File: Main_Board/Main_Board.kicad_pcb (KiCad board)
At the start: 4 copper layers, 45 x 38.4 mm, 124 parts, among them IC1 TPS25200DRVR, J1 RESET, J2 MAIN_UART, J3 Baterry input, J4 External bords interfaces, J7 Terminal, J8 Terminal, Q1 2N7002, Q10 FDN339AN, Q7 MMBT3904LT1G, Q8 FDN339AN, Q9 MMBT3904LT1G, U1 W25Q128JVS, U2 ESP32-S3-MINI-1U, U3 TPS63031DSK, U4 TPS63031DSK, U5 TLV61070ADBV, U6 SS351AT, U7 THVD1450DR

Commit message: Keep out zones, cleanup
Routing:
- net +3V3_MB: track 60.0 -> 18.1 mm
- net GND: track 48.4 -> 45.4 mm
- net Net-(Q8-G): track 33.3 -> 31.0 mm
- net /PSU/Back_Boost1/V_In: track 46.9 -> 45.6 mm

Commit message: Routing + cleanup
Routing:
- net Net-(J4-Pin_1): track 16.3 -> 31.9 mm
- net Net-(U2-RXD0): track 0.00 -> 13.6 mm
- net Net-(U2-TXD0): track 0.00 -> 11.7 mm
- net /ESP32/PYRO2_CONTINUITY: track 2.17 -> 10.2 mm, vias 0 -> 1
- net +3V3_MB: track 18.1 -> 21.6 mm, vias 8 -> 12
- net GND: track 45.4 -> 46.9 mm, vias 23 -> 26
- net Net-(Q10-G): track 32.7 -> 31.9 mm

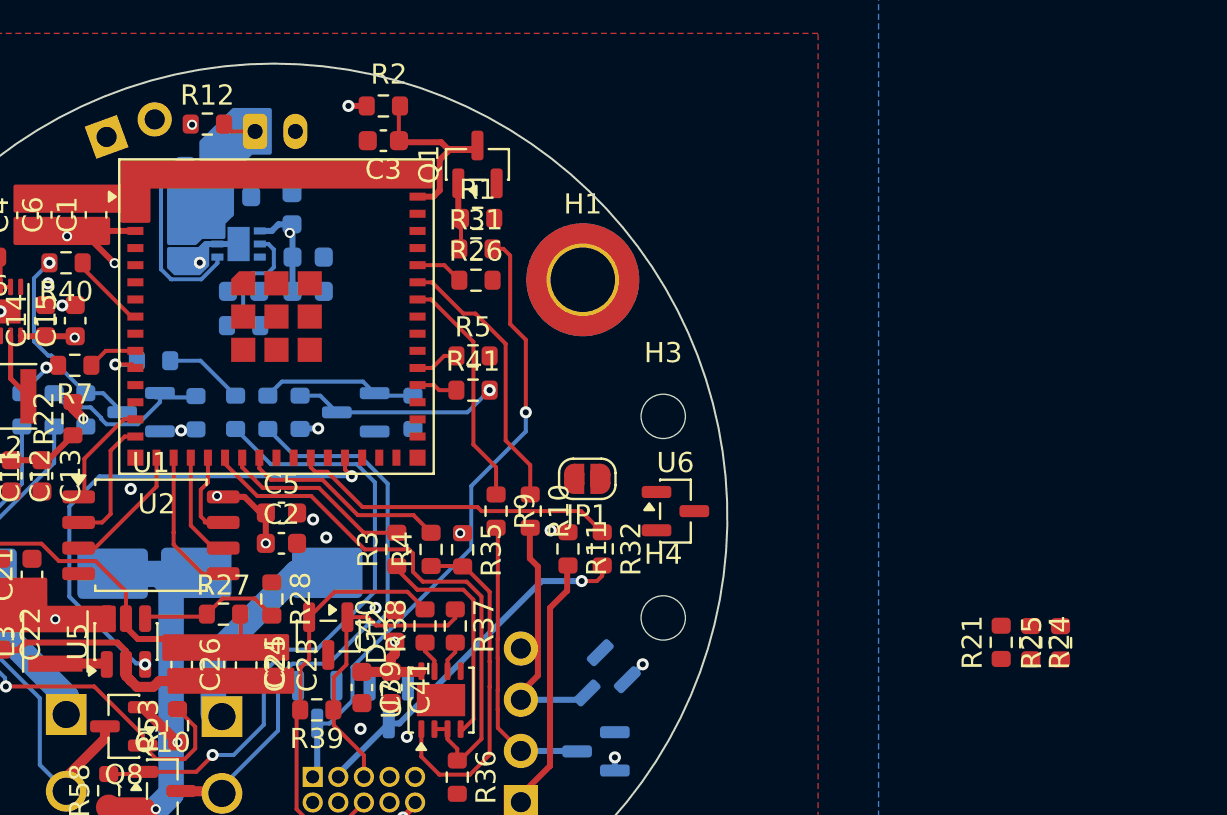
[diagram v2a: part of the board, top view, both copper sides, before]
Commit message: Schematic cleanup, ALED footprint + 3D + sch
+ layout and routing
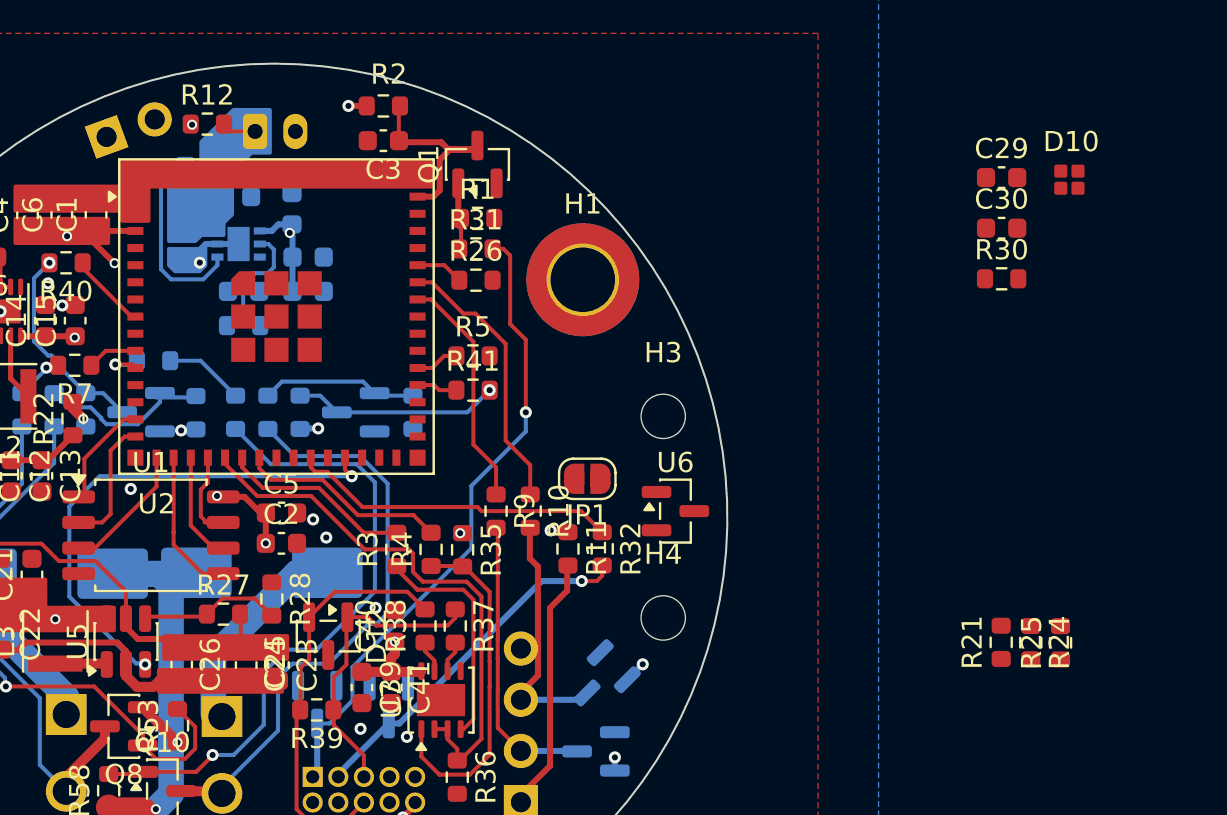
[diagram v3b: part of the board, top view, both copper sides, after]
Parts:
- added C29: 100nF, Capacitor_SMD:C_0603_1608Metric, F.Cu at (136.1, 83.2)
- added C30: 10uF, Capacitor_SMD:C_0603_1608Metric, F.Cu at (136.1, 85.7)
- added D10: SK6812-1515, sk6805-1515:sk68015-1515, F.Cu at (139.5, 83.3)
- added R30: 470R, Resistor_SMD:R_0603_1608Metric, F.Cu at (136.1, 88.2)
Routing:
- net GND: track 46.9 -> 51.3 mm

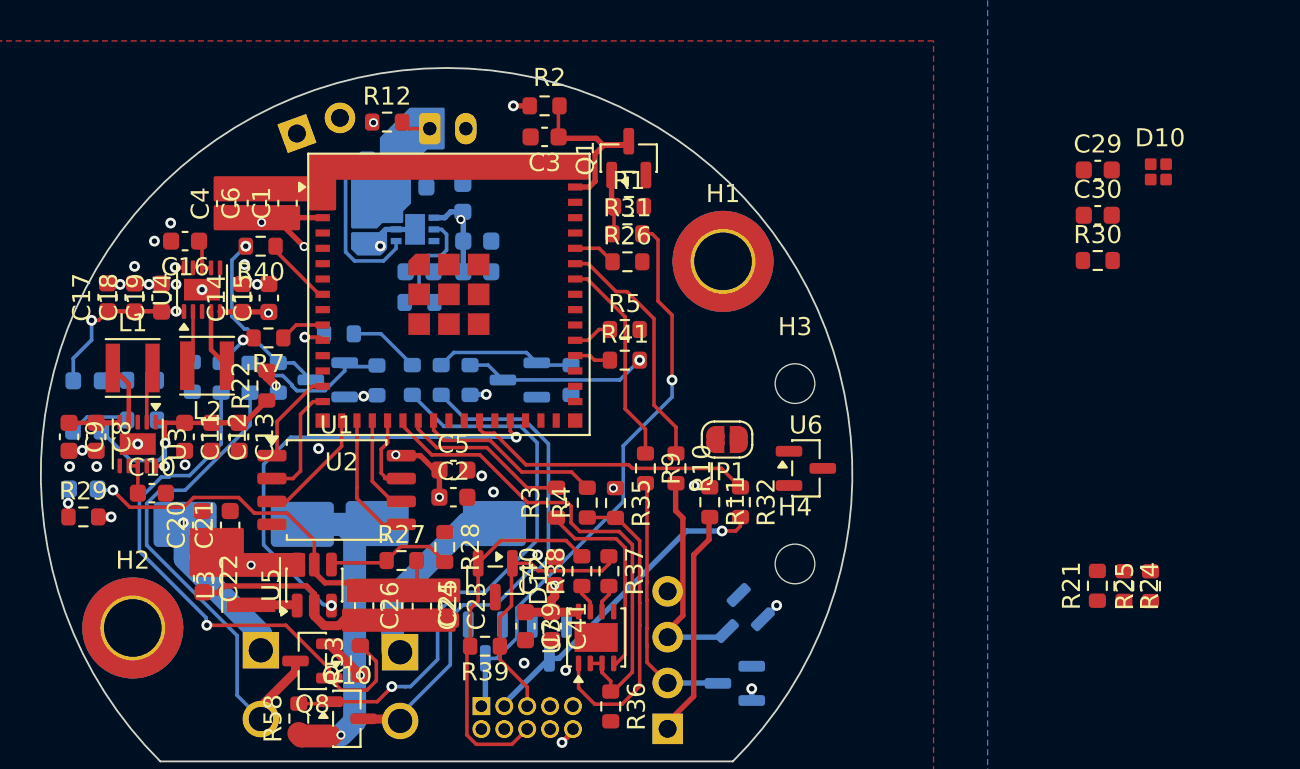
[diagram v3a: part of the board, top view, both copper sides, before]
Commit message: Power routing
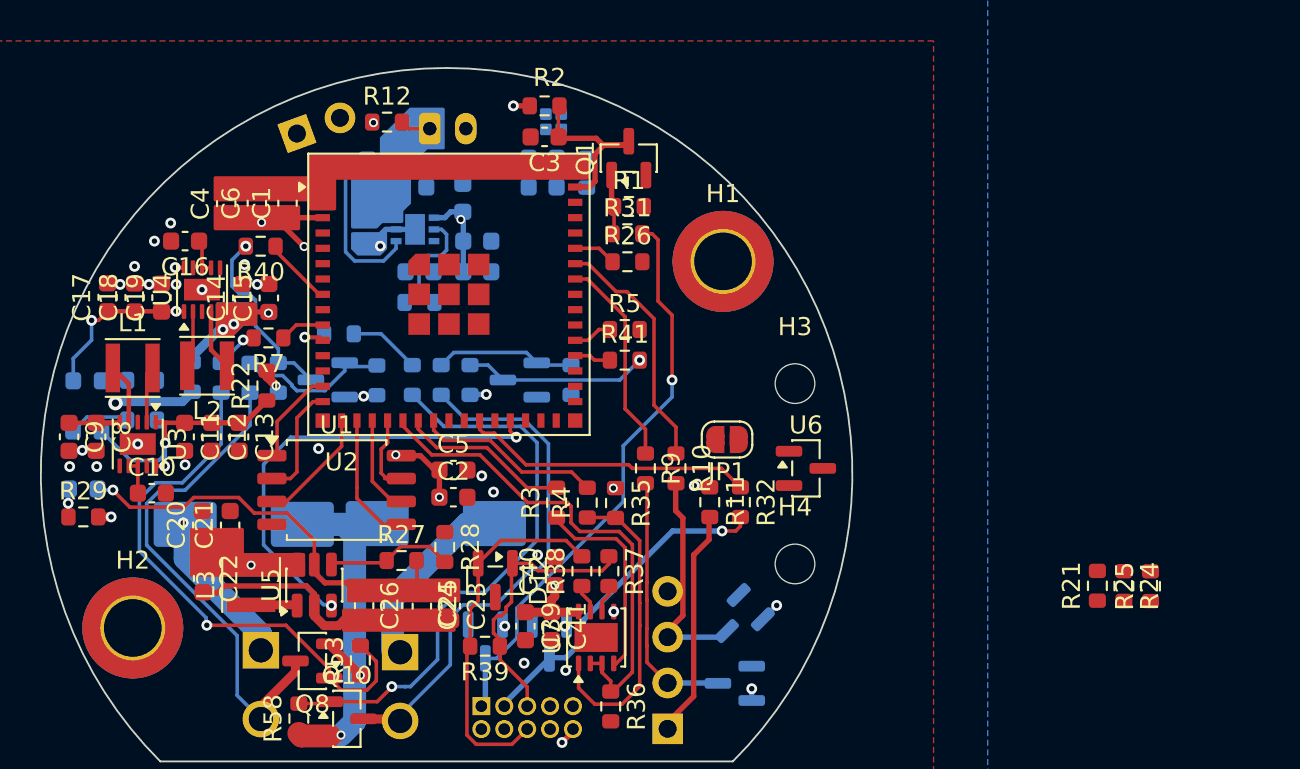
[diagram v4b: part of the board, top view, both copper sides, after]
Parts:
- C29, C30, D10, R30: moved to B.Cu
- moved D10 33.7 mm to (105.9, 80.5)
- moved C30 30.8 mm to (105.3, 84.1), turned to 180 degrees
- moved C29 30.8 mm to (105.3, 82.5), turned to 180 degrees
- moved R30 28.8 mm to (107.8, 83.3), turned to 90 degrees
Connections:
- net Net-(U1-~{HOLD}/~{RESET}/IO_{3}) renamed /ESP32/IO3 / HOLD
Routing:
- net +3V3: track 0.00 -> 8.51 mm, vias 0 -> 2
- net VBUS: track 66.4 -> 70.9 mm, vias 2 -> 3
- net /PSU/Back_Boost1/V_In: track 45.6 -> 49.2 mm, vias 3 -> 5
- net Net-(J4-Pin_3): track 17.9 -> 18.7 mm
- net GND: vias 26 -> 27

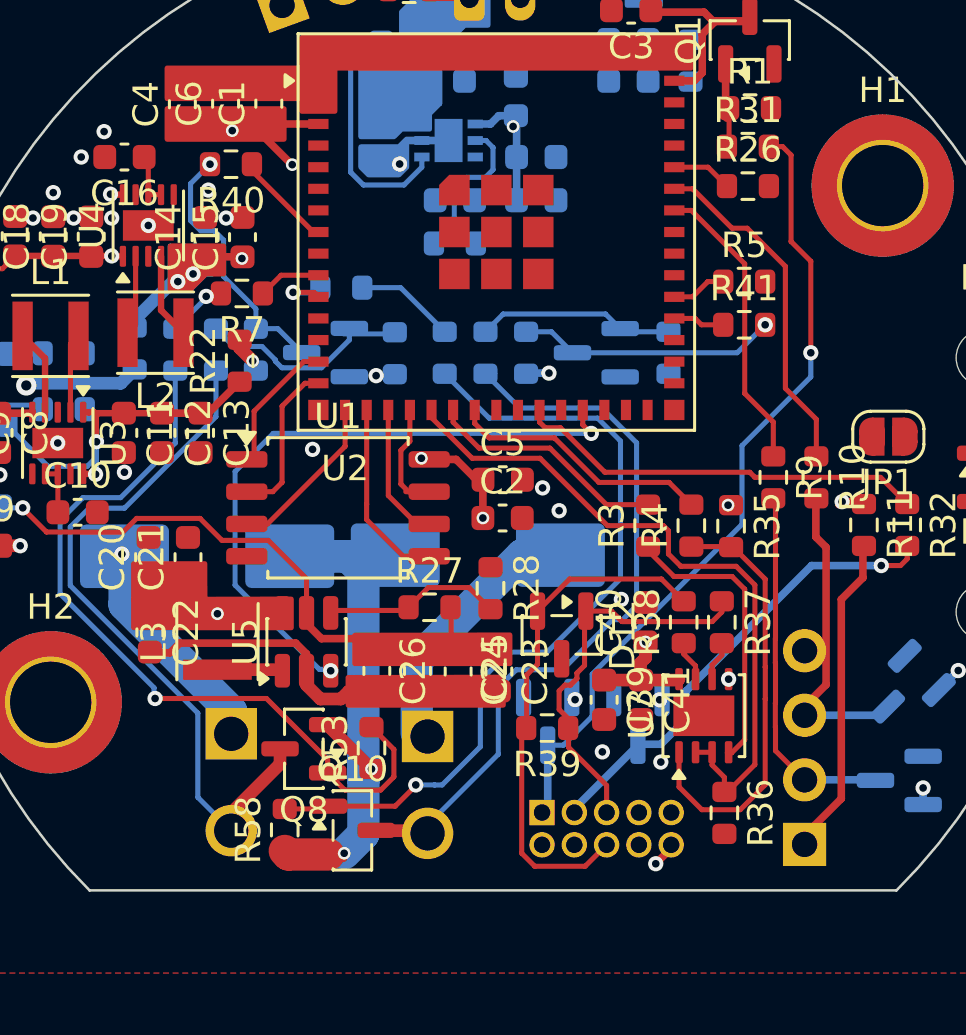
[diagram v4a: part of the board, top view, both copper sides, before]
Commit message: Pyro routing/layout fix
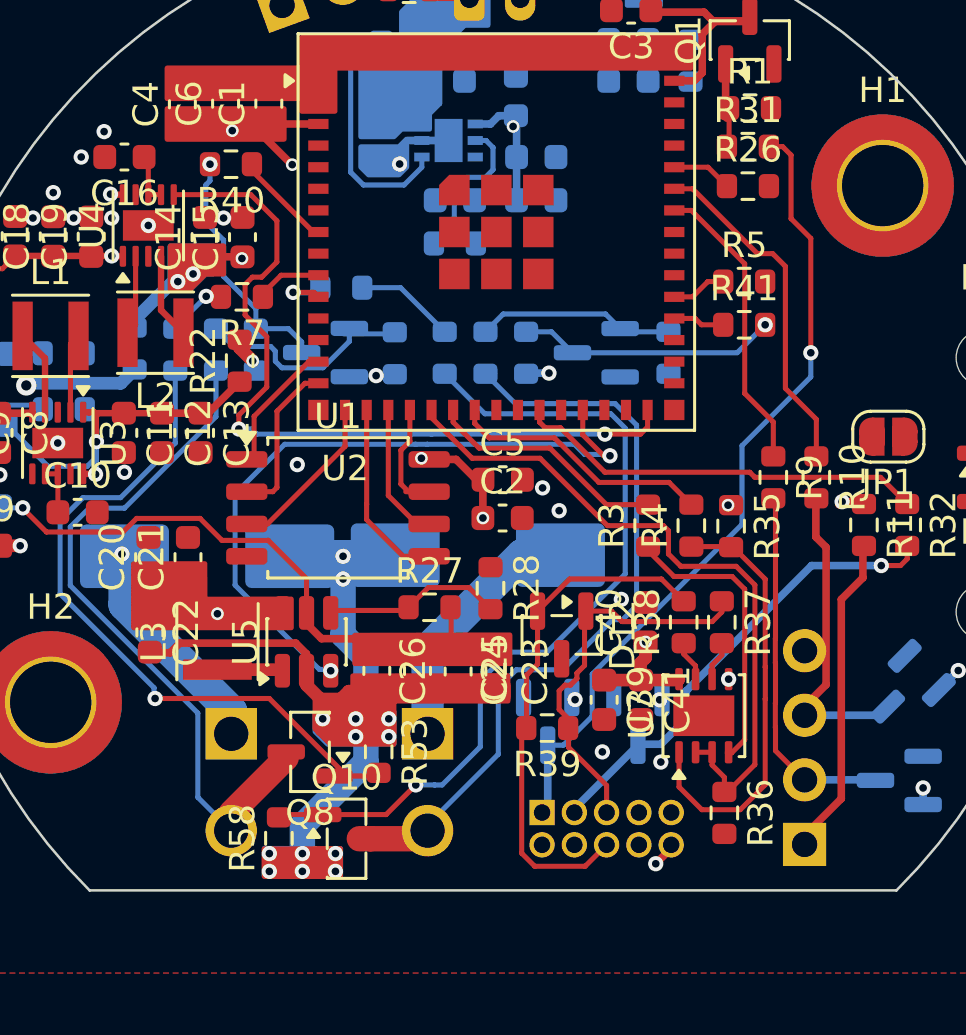
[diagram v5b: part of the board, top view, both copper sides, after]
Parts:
- moved Q10 0.40 mm to (94.2, 113.9)
- moved R58 0.40 mm to (91.6, 113.9)
- moved R53 0.32 mm to (95.5, 110.5), turned to -90 degrees
- moved Q8 0.27 mm to (92.8, 110.5)
- moved R7 0.13 mm to (90.1, 92.6)
- moved J8 0.10 mm to (97.4, 109.8)
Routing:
- net /ESP32/3v3_EN: track 0.00 -> 31.2 mm, vias 0 -> 2
- net GND: track 51.3 -> 46.7 mm, vias 27 -> 37
- net Net-(Q8-G): track 31.2 -> 27.6 mm
- net /ESP32/5V_EN: track 25.3 -> 26.9 mm
- net Net-(J8-Pin_2): track 29.8 -> 30.9 mm
- net Net-(Q10-G): track 31.9 -> 32.9 mm
- net /ESP32/PYRO1_CONTINUITY: track 10.4 -> 9.79 mm

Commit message: ALED
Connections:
- R5 pad 2: /ESP32/LED -> /ESP32/CORE_LED
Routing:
- net /ESP32/CORE_LED: track 0.00 -> 9.08 mm, vias 0 -> 1
- net Net-(D10-DIN): track 0.00 -> 3.48 mm
- net +5V: track 0.00 -> 3.30 mm
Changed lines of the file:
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@@
 			(layers "F.Cu" "F.Mask" "F.Paste")
 			(roundrect_rratio 0.25)
-			(net "/ESP32/LED")
+			(net "/ESP32/CORE_LED")
 			(pintype "passive")
 		)
@@
 	(gr_poly
 		(pts
-			(xy 93 108.9) (xy 93 109.7) (xy 93.5 110.2) (xy 96.1 110.2) (xy 96.1 108.9) (xy 93.5 108.9)
+			(xy 93 108.9) (xy 93 109.6) (xy 93.6 110.2) (xy 96.1 110.2) (xy 96.1 108.9) (xy 93.5 108.9)
 		)
 		(stroke
@@
 	)
 	(segment
+		(start 106.3 80.963787)
+		(end 106.3 81.6)
+		(width 0.3)
+		(layer "B.Cu")
+		(net "+5V")
+	)
+	(segment
+		(start 106.3 81.6)
+		(end 106.1 81.8)
+		(width 0.3)
+		(layer "B.Cu")
+		(net "+5V")
+	)
+	(segment
+		(start 106.1 81.8)
+		(end 106.1 82.5)
+		(width 0.3)
+		(layer "B.Cu")
+		(net "+5V")
+	)
+	(segment
+		(start 106.1 82.5)
+		(end 106.099999 84.1)
+		(width 0.3)
+		(layer "B.Cu")
+		(net "+5V")
+	)
+	(segment
+		(start 106.357893 80.905894)
+		(end 106.3 80.963787)
+		(width 0.3)
+		(layer "B.Cu")
+		(net "+5V")
+	)
+	(segment
 		(start 108.229434 83.786466)
 		(end 107.916017 84.099883)
@@
 	)
 	(segment
-		(start 109.794754 101.54747)
-		(end 103.9 107.442224)
+		(start 103.9 109.1)
+		(end 102.762499 110.237501)
 		(width 0.2)
 		(layer "B.Cu")
@@
 	)
 	(segment
-		(start 102.762499 110.237501)
-		(end 102.15 110.237501)
-		(width 0.2)
+		(start 102.15 112.663379)
+		(end 101.927327 112.886052)
+		(width 0.3)
 		(layer "B.Cu")
 		(net "Net-(J4-Pin_1)")
 	)
 	(segment
-		(start 112.5 94.8)
-		(end 112.5 95.748616)
+		(start 112.5 98.842224)
+		(end 103.9 107.442224)
 		(width 0.2)
 		(layer "B.Cu")
@@
 	)
 	(segment
-		(start 112.5 95.748616)
-		(end 109.794754 98.453862)
+		(start 112.5 94.8)
+		(end 112.5 98.842224)
 		(width 0.2)
 		(layer "B.Cu")
@@
 	)
 	(segment
-		(start 102.15 112.663379)
-		(end 101.927327 112.886052)
-		(width 0.3)
-		(layer "B.Cu")
-		(net "Net-(J4-Pin_1)")
-	)
-	(segment
 		(start 103.9 107.442224)
 		(end 103.9 109.1)
@@
 	)
 	(segment
-		(start 109.794754 98.453862)
-		(end 109.794754 101.54747)
-		(width 0.2)
-		(layer "B.Cu")
-		(net "Net-(J4-Pin_1)")
-	)
-	(segment
-		(start 103.9 109.1)
-		(end 102.762499 110.237501)
+		(start 102.762499 110.237501)
+		(end 102.15 110.237501)
 		(width 0.2)
 		(layer "B.Cu")
@@
 		(net "Net-(IC1-ILIM)")
 	)
+	(segment
+		(start 107.767635 80.667635)
+		(end 107.767635 82.485057)
+		(width 0.2)
+		(layer "B.Cu")
+		(net "Net-(D10-DIN)")
+	)
+	(segment
+		(start 106.357893 80.055894)
+		(end 107.155894 80.055894)
+		(width 0.2)
+		(layer "B.Cu")
+		(net "Net-(D10-DIN)")
+	)
+	(segment
+		(start 107.155894 80.055894)
+		(end 107.767635 80.667635)
+		(width 0.2)
+		(layer "B.Cu")
+		(net "Net-(D10-DIN)")
+	)
+	(via
+		(at 110.7 92)
+		(size 0.6)
+		(drill 0.3)
+		(layers "F.Cu" "B.Cu")
+		(net "/ESP32/CORE_LED")
+	)
+	(segment
+		(start 107.767635 89.067635)
+		(end 110.7 92)
+		(width 0.2)
+		(layer "B.Cu")
+		(net "/ESP32/CORE_LED")
+	)
+	(segment
+		(start 107.767635 84.135057)
+		(end 107.767635 89.067635)
+		(width 0.2)
+		(layer "B.Cu")
+		(net "/ESP32/CORE_LED")
+	)
 	(zone

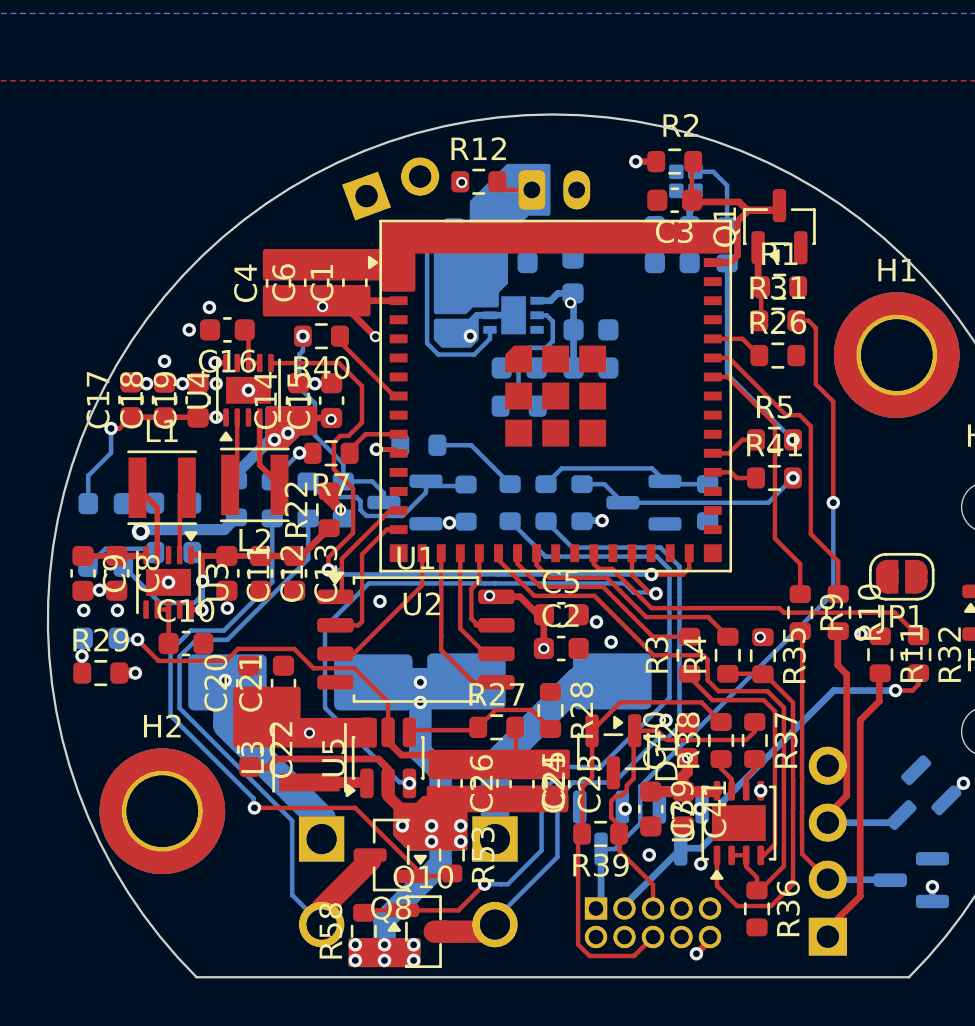
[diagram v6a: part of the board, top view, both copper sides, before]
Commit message: Cleanup + clearance fix
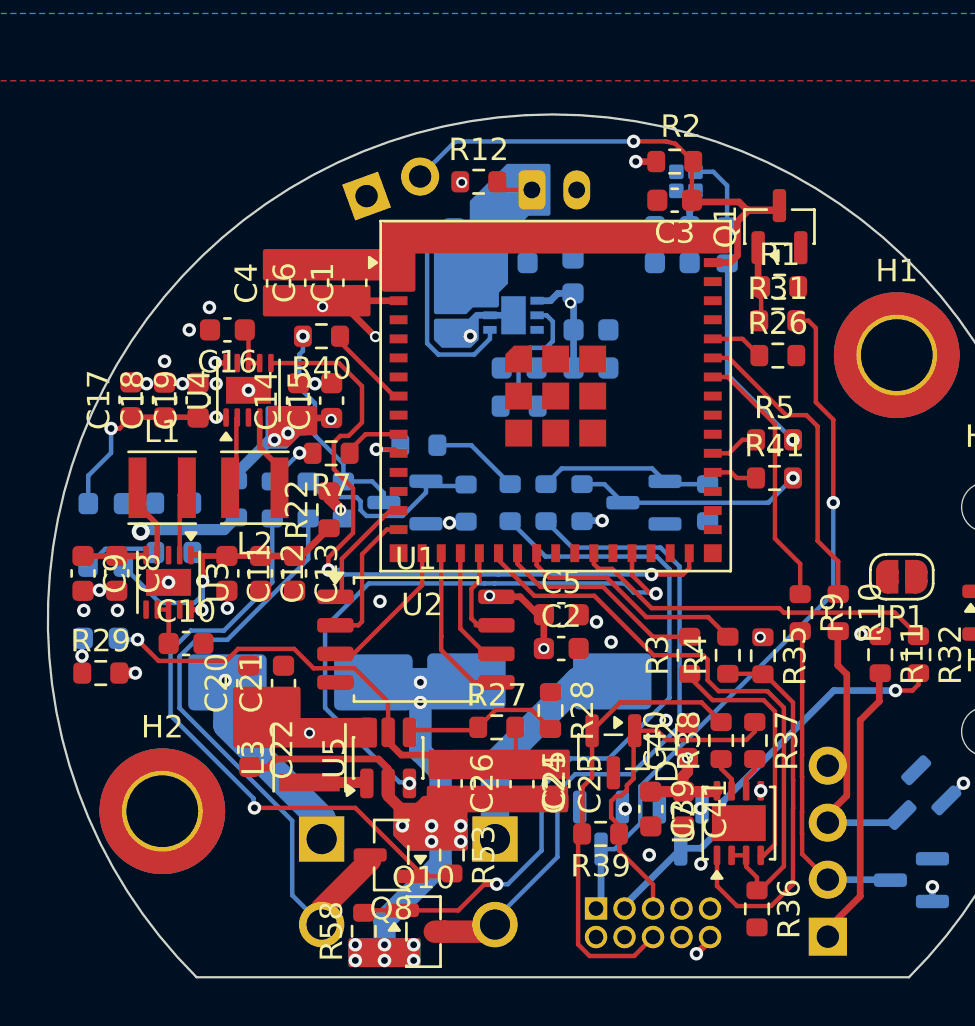
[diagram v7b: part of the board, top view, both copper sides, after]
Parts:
- moved L2 0.13 mm to (86.7, 94.1)
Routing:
- net /ESP32/ESP32_EN: track 10.8 -> 24.1 mm, vias 0 -> 1
- net Net-(Q10-G): track 32.9 -> 33.5 mm
